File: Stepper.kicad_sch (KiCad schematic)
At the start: 10 parts, among them J12 Conn_01x04_Male, U3 TMC2209

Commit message: Rev1. Uart interface
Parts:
- added C14: 10uF, Capacitor_SMD:C_0805_2012Metric, symbol Device:C
- J12: footprint Connector_JST:JST_XH_S4B-XH-A-1_1x04_P2.50mm_Horizontal -> Connector_JST:JST_XH_B4B-XH-A_1x04_P2.50mm_Vertical
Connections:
- net +VDC: now also C14.1
- net GND: now also C14.2
- net at U3.1 (OB2): now also J12.1 (Pin_1); no longer J12.4 (Pin_4)
- net at U3.21 (OA2): now also J12.4 (Pin_4); no longer J12.1 (Pin_1)
- net at U3.24 (OA1): now also J12.3 (Pin_3); no longer J12.2 (Pin_2)
- net at U3.26 (OB1): now also J12.2 (Pin_2); no longer J12.3 (Pin_3)
- net +3V3 renamed +3.3V
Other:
- moved on the sheet: C3, C4, C5, C6, C7, C8, J12, R18, R19, U3

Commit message: Rev2, as ordered
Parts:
- J12: footprint Connector_JST:JST_XH_B4B-XH-A_1x04_P2.50mm_Vertical -> Connector_JST:JST_XH_S4B-XH-A-1_1x04_P2.50mm_Horizontal
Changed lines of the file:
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@@
 		)
 		(property "Value" "10uF"
-			(at 113.411 73.6021 0)
+			(at 113.03 74.93 0)
 			(effects
 				(font
@@
 			)
 		)
-		(property "Footprint" "Connector_JST:JST_XH_B4B-XH-A_1x04_P2.50mm_Vertical"
+		(property "Footprint" "Connector_JST:JST_XH_S4B-XH-A-1_1x04_P2.50mm_Horizontal"
 			(at 177.8 97.79 0)
 			(effects

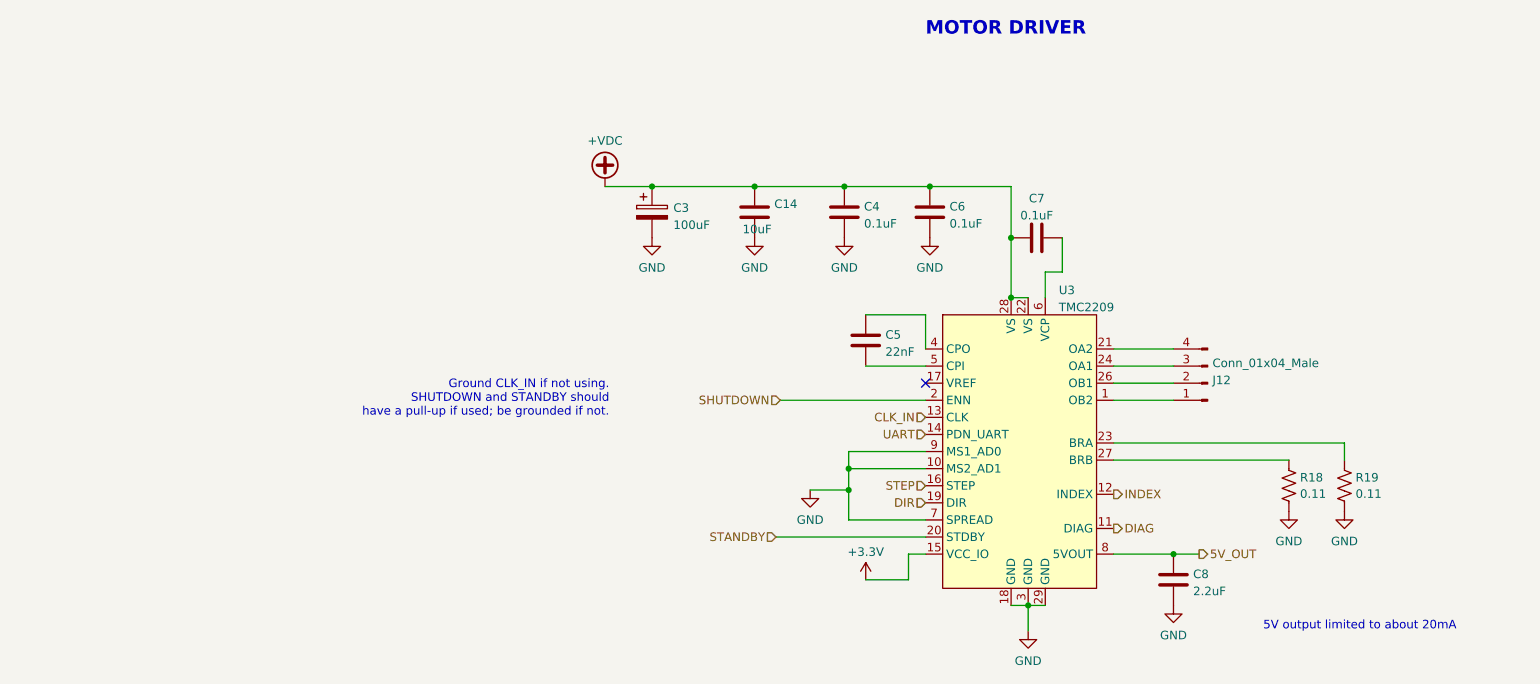
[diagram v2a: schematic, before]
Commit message: Rev3 (connectors on back, and with USB daughter board) - probably done
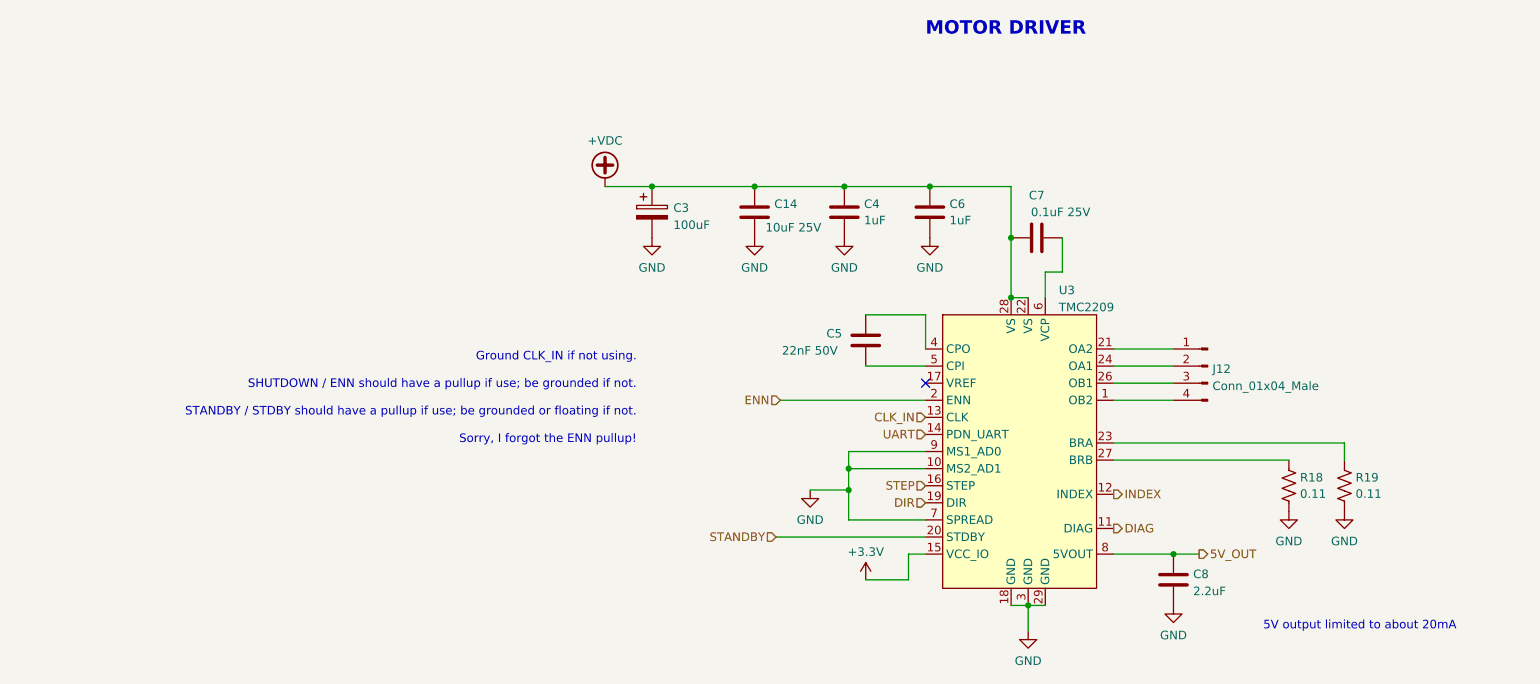
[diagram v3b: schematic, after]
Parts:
- C14: value 10uF -> 10uF 25V
- C3: footprint Capacitor_THT:CP_Radial_D5.0mm_P2.00mm -> Capacitor_THT:CP_Radial_D6.3mm_P2.50mm
- C4, C6: value 0.1uF -> 1uF; footprint Capacitor_SMD:C_0805_2012Metric -> Capacitor_SMD:C_0603_1608Metric
- C5: value 22nF -> 22nF 50V; footprint Capacitor_SMD:C_0805_2012Metric -> Capacitor_SMD:C_0603_1608Metric
- C7: value 0.1uF -> 0.1uF 25V; footprint Capacitor_SMD:C_0805_2012Metric -> Capacitor_SMD:C_0603_1608Metric
- C8: footprint Capacitor_SMD:C_0805_2012Metric -> Capacitor_SMD:C_0603_1608Metric
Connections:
- net at U3.1 (OB2): now also J12.4 (Pin_4); no longer J12.1 (Pin_1)
- net at U3.21 (OA2): now also J12.1 (Pin_1); no longer J12.4 (Pin_4)
- net at U3.24 (OA1): now also J12.2 (Pin_2); no longer J12.3 (Pin_3)
- net at U3.26 (OB1): now also J12.3 (Pin_3); no longer J12.2 (Pin_2)
- net SHUTDOWN renamed ENN
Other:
- note added: "Ground CLK_IN if not using. SHUTDOWN / ENN should have a pullup if use; be grounded if not. STANDBY / STDBY should have a pullup if use; be grounded or floating if not. Sorry, I forgot the ENN pullup!"
- note removed: "Ground CLK_IN if not using. SHUTDOWN and STANDBY should have a pull-up if used; be grounded if not."
- moved on the sheet: J12
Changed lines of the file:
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@@
 		)
 	)
-	(text "Ground CLK_IN if not using.\nSHUTDOWN and STANDBY should\nhave a pull-up if used; be grounded if not."
+	(text "Ground CLK_IN if not using.\n\nSHUTDOWN / ENN should have a pullup if use; be grounded if not.\n\nSTANDBY / STDBY should have a pullup if use; be grounded or floating if not.\n\nSorry, I forgot the ENN pullup!"
 		(exclude_from_sim no)
-		(at 88.9 102.87 0)
+		(at 92.964 106.934 0)
 		(effects
 			(font
@@
 		)
 	)
-	(hierarchical_label "SHUTDOWN"
+	(hierarchical_label "ENN"
 		(shape input)
 		(at 114.3 100.33 180)
@@
 		(on_board yes)
 		(dnp no)
-		(fields_autoplaced yes)
 		(property "Reference" "C7"
-			(at 152.4 70.3412 90)
-			(effects
-				(font
-					(size 1.27 1.27)
-				)
-			)
-		)
-		(property "Value" "0.1uF"
-			(at 152.4 72.8781 90)
-			(effects
-				(font
-					(size 1.27 1.27)
-				)
-			)
-		)
-		(property "Footprint" "Capacitor_SMD:C_0805_2012Metric"
+			(at 152.4 69.8965 90)
+			(effects
+				(font
+					(size 1.27 1.27)
+				)
+			)
+		)
+		(property "Value" "0.1uF 25V"
+			(at 155.956 72.39 90)
+			(effects
+				(font
+					(size 1.27 1.27)
+				)
+			)
+		)
+		(property "Footprint" "Capacitor_SMD:C_0603_1608Metric"
 			(at 156.21 75.2348 0)
 			(effects
@@
 		(fields_autoplaced yes)
 		(property "Reference" "C6"
-			(at 139.446 71.5553 0)
+			(at 139.446 71.1778 0)
 			(effects
 				(font
@@
 			)
 		)
-		(property "Value" "0.1uF"
-			(at 139.446 74.0922 0)
+		(property "Value" "1uF"
+			(at 139.446 73.6021 0)
 			(effects
 				(font
@@
 			)
 		)
-		(property "Footprint" "Capacitor_SMD:C_0805_2012Metric"
+		(property "Footprint" "Capacitor_SMD:C_0603_1608Metric"
 			(at 137.4902 76.2 0)
 			(effects
@@
 			)
 		)
-		(property "Footprint" "Capacitor_THT:CP_Radial_D5.0mm_P2.00mm"
+		(property "Footprint" "Capacitor_THT:CP_Radial_D6.3mm_P2.50mm"
 			(at 96.2152 76.2 0)
 			(effects
@@
 			)
 		)
-		(property "Value" "10uF"
-			(at 113.03 74.93 0)
+		(property "Value" "10uF 25V"
+			(at 120.396 74.676 0)
 			(effects
 				(font
@@
 	(symbol
 		(lib_id "Connector:Conn_01x04_Male")
-		(at 177.8 97.79 180)
+		(at 177.8 95.25 0)
+		(mirror y)
 		(unit 1)
 		(exclude_from_sim no)
@@
 		(dnp no)
 		(property "Reference" "J12"
-			(at 178.5112 97.3547 0)
+			(at 178.5112 95.6853 0)
 			(effects
 				(font
@@
 		)
 		(property "Value" "Conn_01x04_Male"
-			(at 178.5112 94.8178 0)
+			(at 178.5112 98.2222 0)
 			(effects
 				(font
@@
 		)
 		(property "Footprint" "Connector_JST:JST_XH_S4B-XH-A-1_1x04_P2.50mm_Horizontal"
-			(at 177.8 97.79 0)
+			(at 177.8 95.25 0)
 			(effects
 				(font
@@
 		)
 		(property "Datasheet" "~"
-			(at 177.8 97.79 0)
+			(at 177.8 95.25 0)
 			(effects
 				(font
@@
 		)
 		(property "Description" ""
-			(at 177.8 97.79 0)
+			(at 177.8 95.25 0)
 			(effects
 				(font
@@
 		(on_board yes)
 		(dnp no)
-		(fields_autoplaced yes)
 		(property "Reference" "C5"
-			(at 129.921 90.6053 0)
+			(at 121.158 90.424 0)
 			(effects
 				(font
@@
 			)
 		)
-		(property "Value" "22nF"
-			(at 129.921 93.1422 0)
+		(property "Value" "22nF 50V"
+			(at 114.554 92.964 0)
 			(effects
 				(font
@@
 			)
 		)
-		(property "Footprint" "Capacitor_SMD:C_0805_2012Metric"
+		(property "Footprint" "Capacitor_SMD:C_0603_1608Metric"
 			(at 127.9652 95.25 0)
 			(effects
@@
 		(fields_autoplaced yes)
 		(property "Reference" "C4"
-			(at 126.746 71.5553 0)
+			(at 126.746 71.1778 0)
 			(effects
 				(font
@@
 			)
 		)
-		(property "Value" "0.1uF"
-			(at 126.746 74.0922 0)
+		(property "Value" "1uF"
+			(at 126.746 73.6021 0)
 			(effects
 				(font
@@
 			)
 		)
-		(property "Footprint" "Capacitor_SMD:C_0805_2012Metric"
+		(property "Footprint" "Capacitor_SMD:C_0603_1608Metric"
 			(at 124.7902 76.2 0)
 			(effects
@@
 			)
 		)
-		(property "Footprint" "Capacitor_SMD:C_0805_2012Metric"
+		(property "Footprint" "Capacitor_SMD:C_0603_1608Metric"
 			(at 173.6852 130.81 0)
 			(effects

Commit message: Little changes while populating
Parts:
- C3: value 100uF -> 100uF 25V
- C4, C6: value 1uF -> 1uF 25V
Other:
- moved on the sheet: C14, C3, C4
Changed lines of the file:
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@@
 	)
 	(junction
-		(at 95.25 68.58)
+		(at 87.63 68.58)
 		(diameter 0)
 		(color 0 0 0 0)
@@
 	)
 	(junction
-		(at 123.825 68.58)
+		(at 120.65 68.58)
 		(diameter 0)
 		(color 0 0 0 0)
@@
 	)
 	(junction
-		(at 110.49 68.58)
+		(at 104.14 68.58)
 		(diameter 0)
 		(color 0 0 0 0)
@@
 	(wire
 		(pts
-			(xy 88.265 68.58) (xy 95.25 68.58)
-		)
-		(stroke
-			(width 0)
-			(type default)
-		)
-	)
-	(wire
-		(pts
-			(xy 95.25 68.58) (xy 110.49 68.58)
+			(xy 80.645 68.58) (xy 87.63 68.58)
+		)
+		(stroke
+			(width 0)
+			(type default)
+		)
+	)
+	(wire
+		(pts
+			(xy 87.63 68.58) (xy 104.14 68.58)
 		)
 		(stroke
@@
 	(wire
 		(pts
-			(xy 123.825 68.58) (xy 136.525 68.58)
+			(xy 120.65 68.58) (xy 136.525 68.58)
 		)
 		(stroke
@@
 	(wire
 		(pts
-			(xy 110.49 68.58) (xy 123.825 68.58)
+			(xy 104.14 68.58) (xy 120.65 68.58)
 		)
 		(stroke
@@
 			)
 		)
-		(property "Value" "1uF"
+		(property "Value" "1uF 25V"
 			(at 139.446 73.6021 0)
 			(effects
@@
 	(symbol
 		(lib_id "Device:C_Polarized")
-		(at 95.25 72.39 0)
+		(at 87.63 72.39 0)
 		(unit 1)
 		(exclude_from_sim no)
@@
 		(dnp no)
 		(property "Reference" "C3"
-			(at 98.425 71.755 0)
+			(at 90.932 70.8691 0)
 			(effects
 				(font
@@
 			)
 		)
-		(property "Value" "100uF"
-			(at 98.425 74.2919 0)
+		(property "Value" "100uF 25V"
+			(at 90.932 73.406 0)
 			(effects
 				(font
@@
 		)
 		(property "Footprint" "Capacitor_THT:CP_Radial_D6.3mm_P2.50mm"
-			(at 96.2152 76.2 0)
+			(at 88.5952 76.2 0)
 			(effects
 				(font
@@
 		)
 		(property "Datasheet" "~"
-			(at 95.25 72.39 0)
+			(at 87.63 72.39 0)
 			(effects
 				(font
@@
 		)
 		(property "Description" ""
-			(at 95.25 72.39 0)
+			(at 87.63 72.39 0)
 			(effects
 				(font
@@
 	(symbol
 		(lib_id "power:GND")
-		(at 123.825 76.2 0)
+		(at 120.65 76.2 0)
 		(unit 1)
 		(exclude_from_sim no)
@@
 		(fields_autoplaced yes)
 		(property "Reference" "#PWR017"
-			(at 123.825 82.55 0)
+			(at 120.65 82.55 0)
 			(effects
 				(font
@@
 		)
 		(property "Value" "GND"
-			(at 123.825 80.6434 0)
+			(at 120.65 80.6434 0)
 			(effects
 				(font
@@
 		)
 		(property "Footprint" ""
-			(at 123.825 76.2 0)
+			(at 120.65 76.2 0)
 			(effects
 				(font
@@
 		)
 		(property "Datasheet" ""
-			(at 123.825 76.2 0)
+			(at 120.65 76.2 0)
 			(effects
 				(font
@@
 		)
 		(property "Description" ""
-			(at 123.825 76.2 0)
+			(at 120.65 76.2 0)
 			(effects
 				(font
@@
 	(symbol
 		(lib_id "power:GND")
-		(at 110.49 76.2 0)
+		(at 104.14 76.2 0)
 		(unit 1)
 		(exclude_from_sim no)
@@
 		(fields_autoplaced yes)
 		(property "Reference" "#PWR025"
-			(at 110.49 82.55 0)
+			(at 104.14 82.55 0)
 			(effects
 				(font
@@
 		)
 		(property "Value" "GND"
-			(at 110.49 80.6434 0)
+			(at 104.14 80.6434 0)
 			(effects
 				(font
@@
 		)
 		(property "Footprint" ""
-			(at 110.49 76.2 0)
+			(at 104.14 76.2 0)
 			(effects
 				(font
@@
 		)
 		(property "Datasheet" ""
-			(at 110.49 76.2 0)
+			(at 104.14 76.2 0)
 			(effects
 				(font
@@
 		)
 		(property "Description" ""
-			(at 110.49 76.2 0)
+			(at 104.14 76.2 0)
 			(effects
 				(font
@@
 	(symbol
 		(lib_id "power:GND")
-		(at 95.25 76.2 0)
+		(at 87.63 76.2 0)
 		(unit 1)
 		(exclude_from_sim no)
@@
 		(fields_autoplaced yes)
 		(property "Reference" "#PWR014"
-			(at 95.25 82.55 0)
+			(at 87.63 82.55 0)
 			(effects
 				(font
@@
 		)
 		(property "Value" "GND"
-			(at 95.25 80.6434 0)
+			(at 87.63 80.6434 0)
 			(effects
 				(font
@@
 		)
 		(property "Footprint" ""
-			(at 95.25 76.2 0)
+			(at 87.63 76.2 0)
 			(effects
 				(font
@@
 		)
 		(property "Datasheet" ""
-			(at 95.25 76.2 0)
+			(at 87.63 76.2 0)
 			(effects
 				(font
@@
 		)
 		(property "Description" ""
-			(at 95.25 76.2 0)
+			(at 87.63 76.2 0)
 			(effects
 				(font
@@
 	(symbol
 		(lib_id "Device:C")
-		(at 110.49 72.39 0)
+		(at 104.14 72.39 0)
 		(unit 1)
 		(exclude_from_sim no)
@@
 		(dnp no)
 		(property "Reference" "C14"
-			(at 113.411 71.1778 0)
+			(at 107.061 71.1778 0)
 			(effects
 				(font
@@
 		)
 		(property "Value" "10uF 25V"
-			(at 120.396 74.676 0)
+			(at 116.332 73.66 0)
 			(effects
 				(font
@@
 		)
 		(property "Footprint" "Capacitor_SMD:C_0805_2012Metric"
-			(at 111.4552 76.2 0)
+			(at 105.1052 76.2 0)
 			(effects
 				(font
@@
 		)
 		(property "Datasheet" "~"
-			(at 110.49 72.39 0)
+			(at 104.14 72.39 0)
 			(effects
 				(font
@@
 		)
 		(property "Description" ""
-			(at 110.49 72.39 0)
+			(at 104.14 72.39 0)
 			(effects
 				(font
@@
 	(symbol
 		(lib_id "power:+VDC")
-		(at 88.265 68.58 0)
+		(at 80.645 68.58 0)
 		(unit 1)
 		(exclude_from_sim no)
@@
 		(fields_autoplaced yes)
 		(property "Reference" "#PWR028"
-			(at 88.265 71.12 0)
+			(at 80.645 71.12 0)
 			(effects
 				(font
@@
 		)
 		(property "Value" "+VDC"
-			(at 88.265 61.7799 0)
+			(at 80.645 61.7799 0)
 			(effects
 				(font
@@
 		)
 		(property "Footprint" ""
-			(at 88.265 68.58 0)
+			(at 80.645 68.58 0)
 			(effects
 				(font
@@
 		)
 		(property "Datasheet" ""
-			(at 88.265 68.58 0)
+			(at 80.645 68.58 0)
 			(effects
 				(font
@@
 		)
 		(property "Description" ""
-			(at 88.265 68.58 0)
+			(at 80.645 68.58 0)
 			(effects
 				(font
@@
 	(symbol
 		(lib_id "Device:C")
-		(at 123.825 72.39 0)
+		(at 120.65 72.39 0)
 		(unit 1)
 		(exclude_from_sim no)
@@
 		(fields_autoplaced yes)
 		(property "Reference" "C4"
-			(at 126.746 71.1778 0)
+			(at 123.571 71.1778 0)
 			(effects
 				(font
@@
 			)
 		)
-		(property "Value" "1uF"
-			(at 126.746 73.6021 0)
+		(property "Value" "1uF 25V"
+			(at 123.571 73.6021 0)
 			(effects
 				(font
@@
 		)
 		(property "Footprint" "Capacitor_SMD:C_0603_1608Metric"
-			(at 124.7902 76.2 0)
+			(at 121.6152 76.2 0)
 			(effects
 				(font
@@
 		)
 		(property "Datasheet" "~"
-			(at 123.825 72.39 0)
+			(at 120.65 72.39 0)
 			(effects
 				(font
@@
 		)
 		(property "Description" ""
-			(at 123.825 72.39 0)
-			(effects
-				(font
+			(at 120.65 72.39 0)
+			(effects
+				(font
